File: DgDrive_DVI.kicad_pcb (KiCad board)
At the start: 2 copper layers, 69 x 28 mm, 26 parts, among them J1 Bias-T, J2 DVI-I, J3 Ld+, J4 Ld-, J5 Pz+, J6 Pz-, J7 Piezo_In, K1 G6AU, Q1 MMBT3904, Q2 2N4401

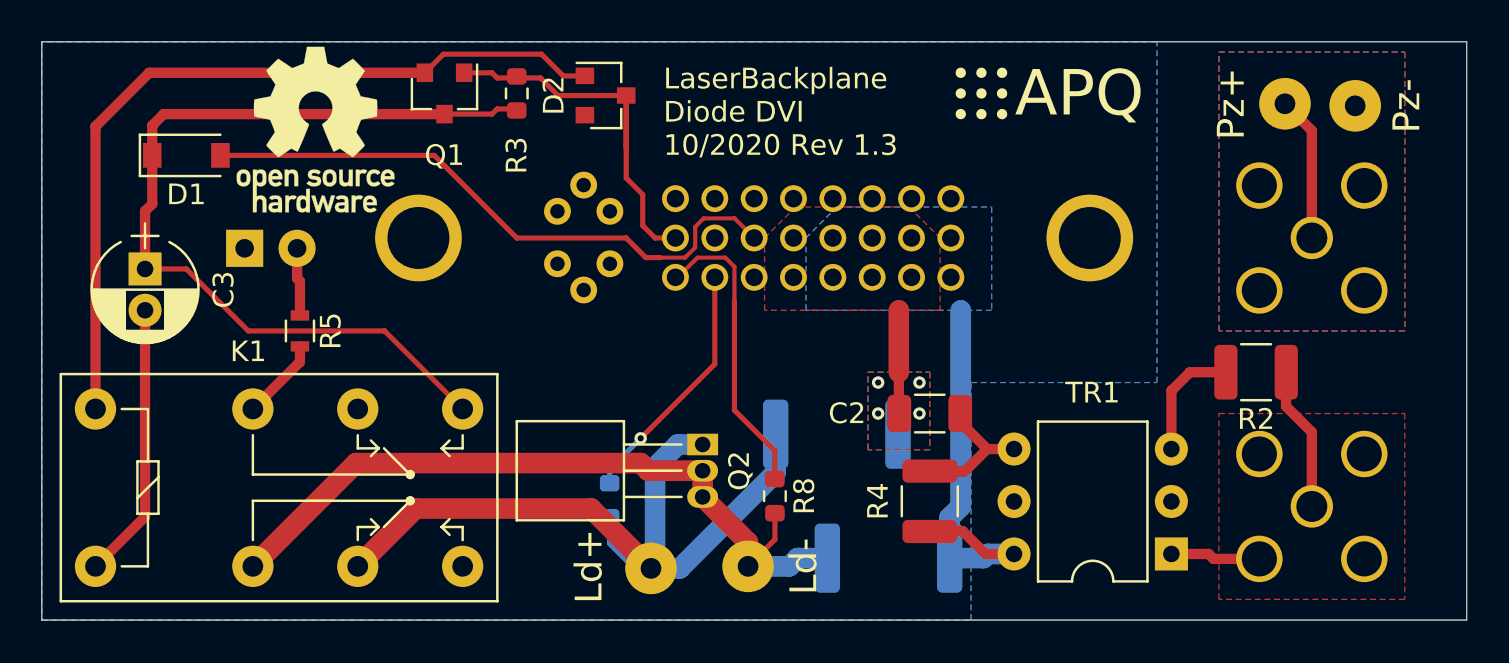
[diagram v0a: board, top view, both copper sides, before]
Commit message: Ld-: SMD Pad for shield
Fix footprints and replace Ld- THT with SMD pad
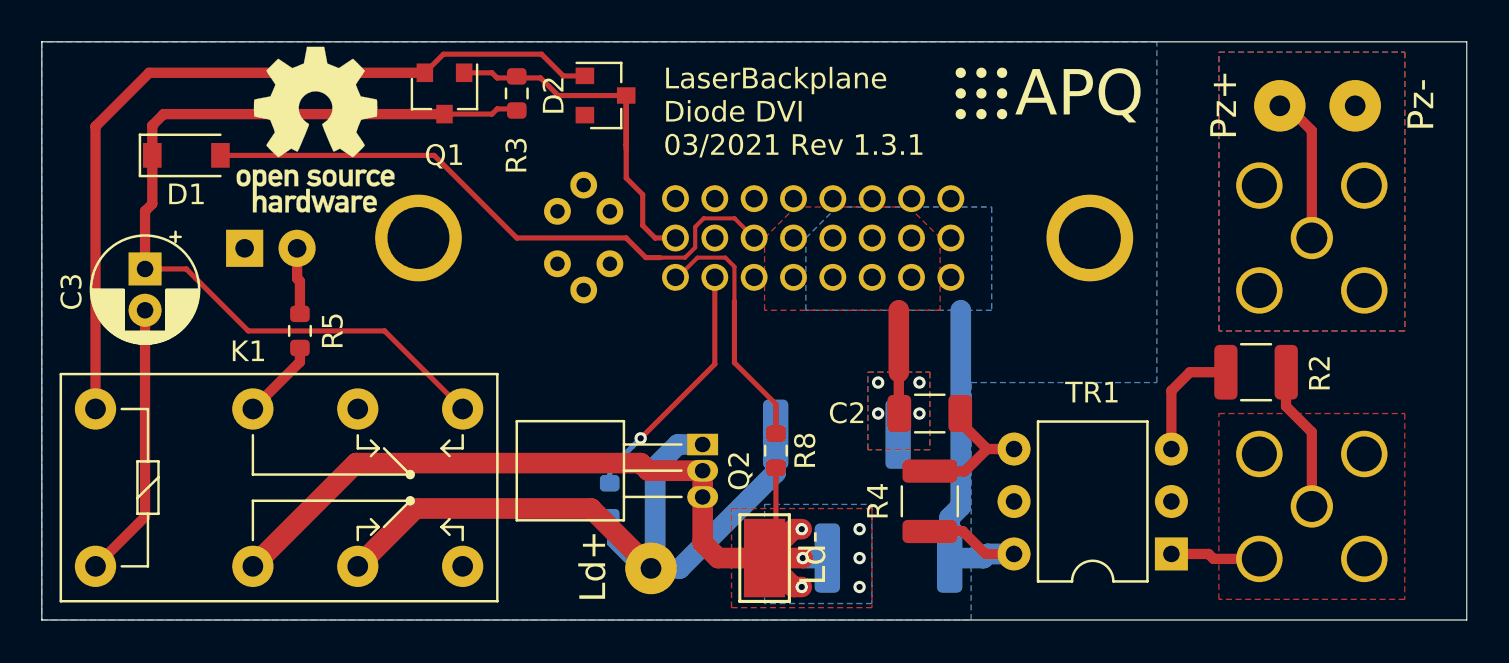
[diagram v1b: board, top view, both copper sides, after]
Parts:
- C3: footprint Capacitors_THT:CP_Radial_D5.0mm_P2.00mm -> Capacitor_THT:CP_Radial_D5.0mm_P2.00mm
- J3, J5, J6: footprint Wire_Pads:SolderWirePad_single_1mmDrill -> Connector_Wire:SolderWirePad_1x01_Drill1mm
- J4: footprint Wire_Pads:SolderWirePad_single_1mmDrill -> TestPoint:TestPoint_Keystone_5019_Minature
- R5: value 2k -> 1k; footprint Resistors_SMD:R_0603 -> Resistor_SMD:R_0603_1608Metric
- moved R8 2.20 mm to (125.5, 109.8)
- moved J4 0.89 mm to (125.0, 115.0), turned to 90 degrees
- moved J5 0.27 mm to (149.9, 93.1)
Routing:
- net LD_short-: track 36.7 -> 45.0 mm, vias 0 -> 6
- net V_diode-: track 14.5 -> 12.4 mm
- added copper zone on B.Cu, net LD_short-
- added copper zone on F.Cu, net LD_short-
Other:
- board text added: "LaserBackplane Diode DVI 03/2021 Rev 1.3.1"
- board text removed: "LaserBackplane Diode DVI 10/2020 Rev 1.3"

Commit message: Add current source
Replace Bias-T with Howland current source. The current source requires additional negative supply (Pin7).

Replace large resistors with inductors+49.9-resistors.
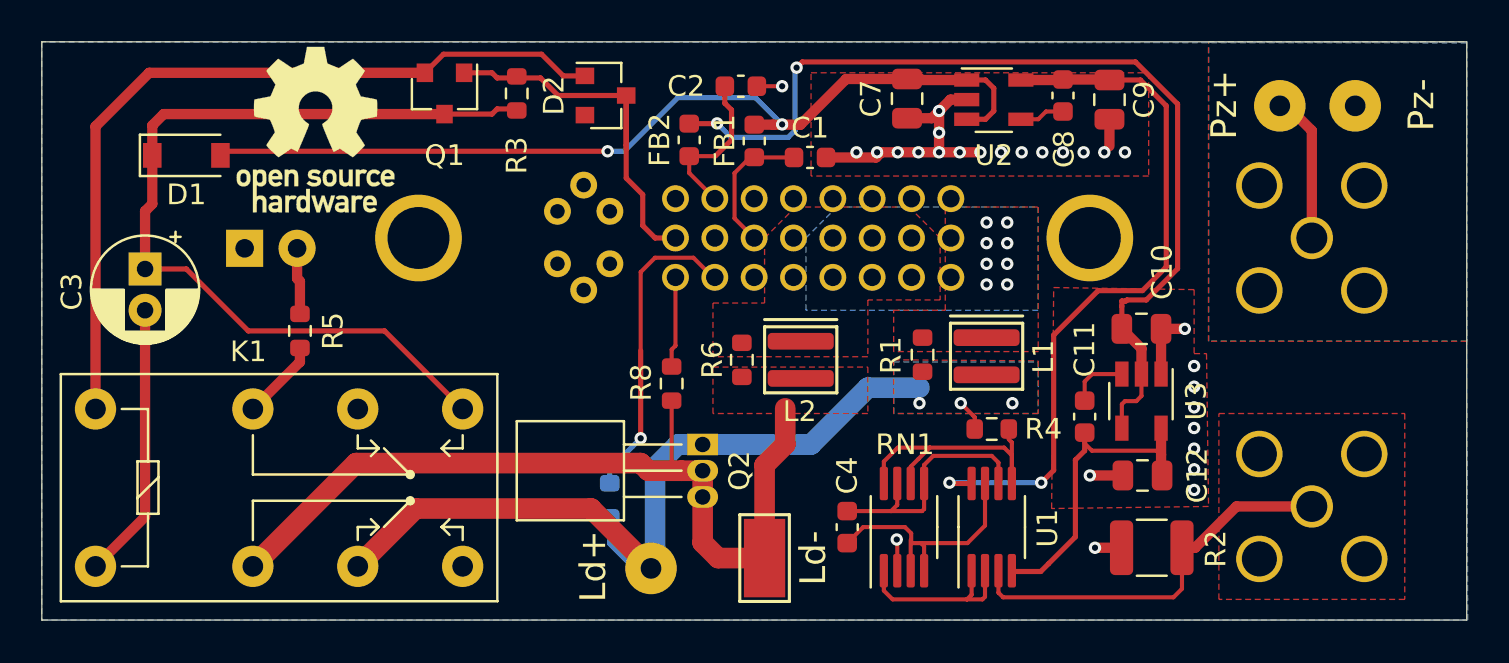
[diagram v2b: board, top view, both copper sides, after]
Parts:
- removed TR1: SWB1010, Package_DIP:DIP-6_W7.62mm
- added C1: 10n, Capacitor_SMD:C_0603_1608Metric, F.Cu at (127.2, 95.6)
- added C10: 4.7u, Capacitor_SMD:C_0805_2012Metric, F.Cu at (143.2, 103.9)
- added C11: 10n, Capacitor_SMD:C_0603_1608Metric, F.Cu at (140.5, 108.2)
- added C12: 4.7u, Capacitor_SMD:C_0805_2012Metric, F.Cu at (143.3, 111.0)
- added C4: 1.5p, Capacitor_SMD:C_0603_1608Metric, F.Cu at (129.0, 113.5)
- added C7: 4.7u, Capacitor_SMD:C_0805_2012Metric, F.Cu at (131.9, 92.8)
- added C8: 10n, Capacitor_SMD:C_0603_1608Metric, F.Cu at (139.4, 92.6)
- added C9: 4.7u, Capacitor_SMD:C_0805_2012Metric, F.Cu at (141.7, 92.8)
- added FB1: BLM18KG102SZ1D, Inductor_SMD:L_0603_1608Metric, F.Cu at (124.5, 94.8)
- added FB2: BLM18KG102SZ1D, Inductor_SMD:L_0603_1608Metric, F.Cu at (121.3, 94.8)
- added L1: 3.3u, custom:Coilcraft_XGL3530, F.Cu at (135.8, 104.3)
- added L2: 3.3u, custom:Coilcraft_XGL3530, F.Cu at (126.8, 104.5)
- added RN1: 10k, custom:MSOP-8_3x3mm_P0.65mm_mod, F.Cu at (131.8, 113.5)
- added U1: ADA4807-2ARM, custom:MSOP-8_3x3mm_P0.65mm_mod, F.Cu at (136.0, 113.5)
- added U2: LT1761-5, Package_TO_SOT_SMD:TSOT-23-5, F.Cu at (136.1, 92.8)
- added U3: LT1964-5, Package_TO_SOT_SMD:TSOT-23-5, F.Cu at (143.2, 107.4)
- C2: value 3.3n (C0G) -> 10n; footprint Capacitor_SMD:C_1206_3216Metric -> Capacitor_SMD:C_0603_1608Metric
- J1: value Bias-T -> Curr. Mod.
- LOGO1: moved to B.Cu
- R1, R6: value 5.6 / 750 mW -> 49.9; footprint Resistor_SMD:R_2512_6332Metric -> Resistor_SMD:R_0603_1608Metric; moved to F.Cu
- R4: value 49.9 -> 10; footprint Resistor_SMD:R_1210_3225Metric -> Resistor_SMD:R_0603_1608Metric
- moved LOGO1 25.5 mm to (144.1, 115.2)
- moved C2 18.3 mm to (123.8, 92.2)
- moved R6 11.9 mm to (123.9, 105.4), turned to 90 degrees
- moved R2 9.89 mm to (143.8, 114.5)
- moved R8 6.01 mm to (120.5, 106.5)
- moved R1 5.66 mm to (132.7, 105.2), turned to 90 degrees
- moved R4 4.61 mm to (136.0, 108.8), turned to 180 degrees
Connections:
- C2 pad 2: Net-(C2-Pad2) -> GND
- D1 pad 2: Relay+ -> +12V
- J1 pad 2: Net-(J1-Pad2) -> GND
- J2 pad 10: Net-(C2-Pad1) -> Net-(J2-Pad10)
- J2 pad 13: Net-(C2-Pad1) -> Net-(J2-Pad10)
- J2 pad 14: Relay+ -> Net-(C1-Pad1)
- J2 pad 7: Net-(J2-Pad7) -> Net-(C2-Pad1)
- J3 pad 1: LD_short+ -> Curr_Mod
- K1 pad 6: LD_short+ -> Curr_Mod
- Q2 pad 1: LD_short+ -> Curr_Mod
- R1 pad 1: LD_short+ -> Curr_Mod
- R1 pad 2: Net-(C2-Pad1) -> Net-(J2-Pad12)
- R2 pad 2: Net-(R2-Pad2) -> GND
- R4 pad 1: Net-(C2-Pad2) -> Net-(R4-Pad1)
- R4 pad 2: Net-(J2-Pad12) -> Curr_Mod
- R6 pad 2: Net-(J2-Pad12) -> Net-(J2-Pad10)
- R7 pad 1: LD_short+ -> Curr_Mod
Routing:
- net -12V: track 0.00 -> 46.6 mm, vias 0 -> 2
- net +12V: track 0.00 -> 44.6 mm, vias 0 -> 2
- net Curr_Mod: track 0.00 -> 41.2 mm, vias 0 -> 3
- net LD_short+: track 37.9 -> 0.00 mm
- net +5V: track 0.00 -> 35.1 mm, vias 0 -> 2
- net Relay+: track 29.7 -> 0.00 mm
- net GND: track 0.00 -> 23.1 mm, vias 0 -> 28
- net Net-(J2-Pad12): track 20.2 -> 0.00 mm, vias 0 -> 8
- net -5V: track 0.00 -> 15.8 mm
- net Net-(R4-Pad1): track 0.00 -> 13.8 mm
- net Net-(C4-Pad1): track 0.00 -> 12.9 mm
- net Net-(J1-Pad1): track 7.02 -> 19.3 mm
- net Net-(C4-Pad2): track 0.00 -> 12.3 mm
- net Net-(RN1-Pad1): track 0.00 -> 8.76 mm
- net V_diode-: track 12.4 -> 4.51 mm
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- added copper zone on B.Cu, net Curr_Mod
- added copper zone on F.Cu, net Curr_Mod
- added copper zone on F.Cu, net GND
- added copper zone on F.Cu, net Net-(J2-Pad10)
- added copper zone on F.Cu, net Net-(J2-Pad12)
- removed copper zone on B.Cu, net LD_short-
- removed copper zone on B.Cu, net Net-(C2-Pad1)
- removed copper zone on F.Cu, net Net-(C2-Pad1)
- removed copper zone on F.Cu, net Net-(J1-Pad2)
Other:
- board text added: "LaserBackplane Diode DVI 03/2021 Rev 1.4"
- board text removed: "Distance of the back side to the case: 0.9 mm"
- board text removed: "LaserBackplane Diode DVI 03/2021 Rev 1.3.1"
- board text removed: "Note: The two big 2512 resistors will be thermally coupled to the case, so they need to be on the back side"

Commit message: Updated Gerber files to 1.4 Added EEPROM
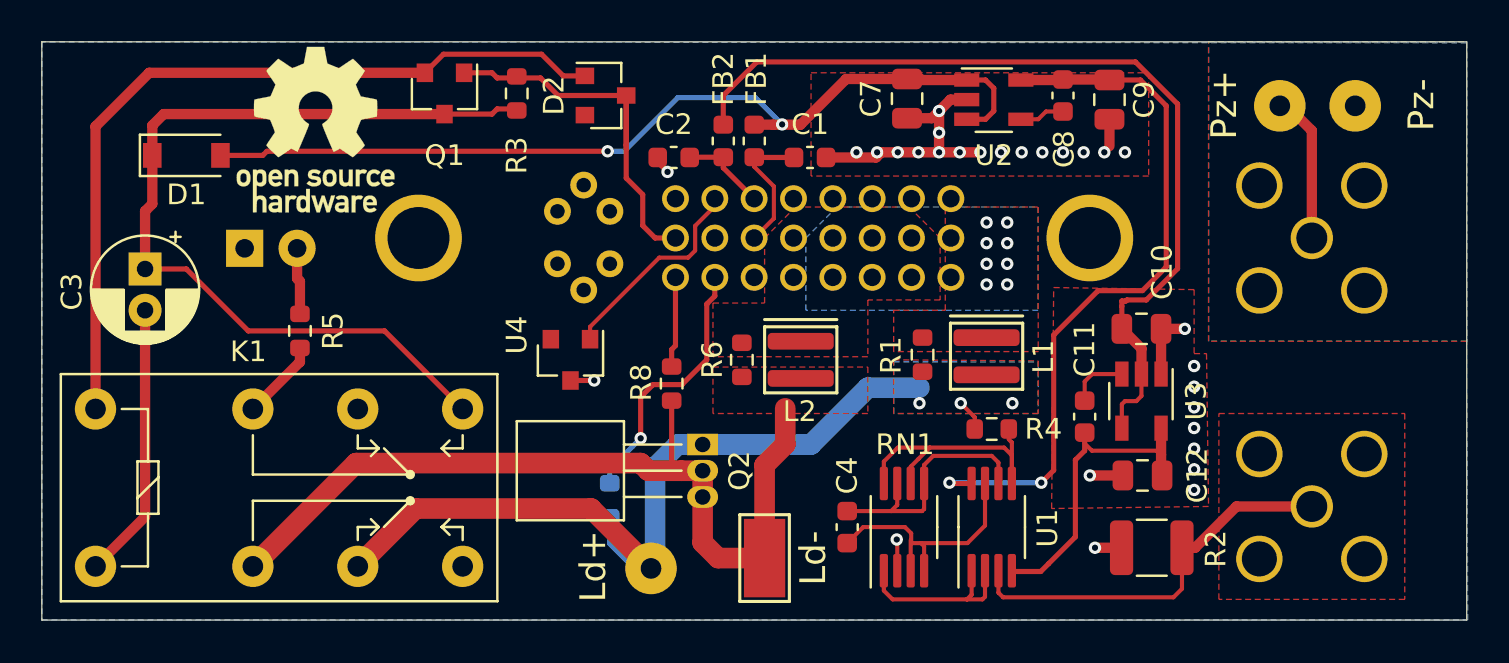
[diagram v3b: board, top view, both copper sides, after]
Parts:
- added U4: AT21CS11-STXXXX-X, Package_TO_SOT_SMD:SOT-23, F.Cu at (115.6, 105.4)
- moved C2 4.74 mm to (120.6, 95.6), turned to 180 degrees
- moved FB2 1.65 mm to (123.0, 94.8)
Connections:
- J2 pad 6: Net-(J2-Pad6) -> Net-(C2-Pad1)
- J2 pad 7: Net-(C2-Pad1) -> Net-(J2-Pad7)
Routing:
- net Net-(J2-Pad7): track 0.00 -> 10.1 mm
- net Net-(C2-Pad1): track 7.68 -> 4.26 mm
- net -12V: track 46.6 -> 43.5 mm, vias 2 -> 0
- net V_diode+: track 15.2 -> 12.9 mm
- net GND: track 23.1 -> 23.9 mm, vias 28 -> 29

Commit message: Fix laser diode polarity
Switch LD-/LD+ pins at the DVI connector
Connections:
- L1 pad 1: Net-(J2-Pad12) -> Net-(J2-Pad10)
- L2 pad 1: Net-(J2-Pad10) -> Net-(J2-Pad12)
- R1 pad 2: Net-(J2-Pad12) -> Net-(J2-Pad10)
- R6 pad 2: Net-(J2-Pad10) -> Net-(J2-Pad12)
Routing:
- net Net-(J2-Pad12): vias 8 -> 0
- net Net-(J2-Pad10): vias 0 -> 8
- added copper zone on B.Cu, net Net-(J2-Pad10)
- removed copper zone on B.Cu, net Net-(J2-Pad12)
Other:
- board text added: "LaserBackplane Diode DVI 07/2021 Rev 1.5"
- board text removed: "LaserBackplane Diode DVI 03/2021 Rev 1.4"

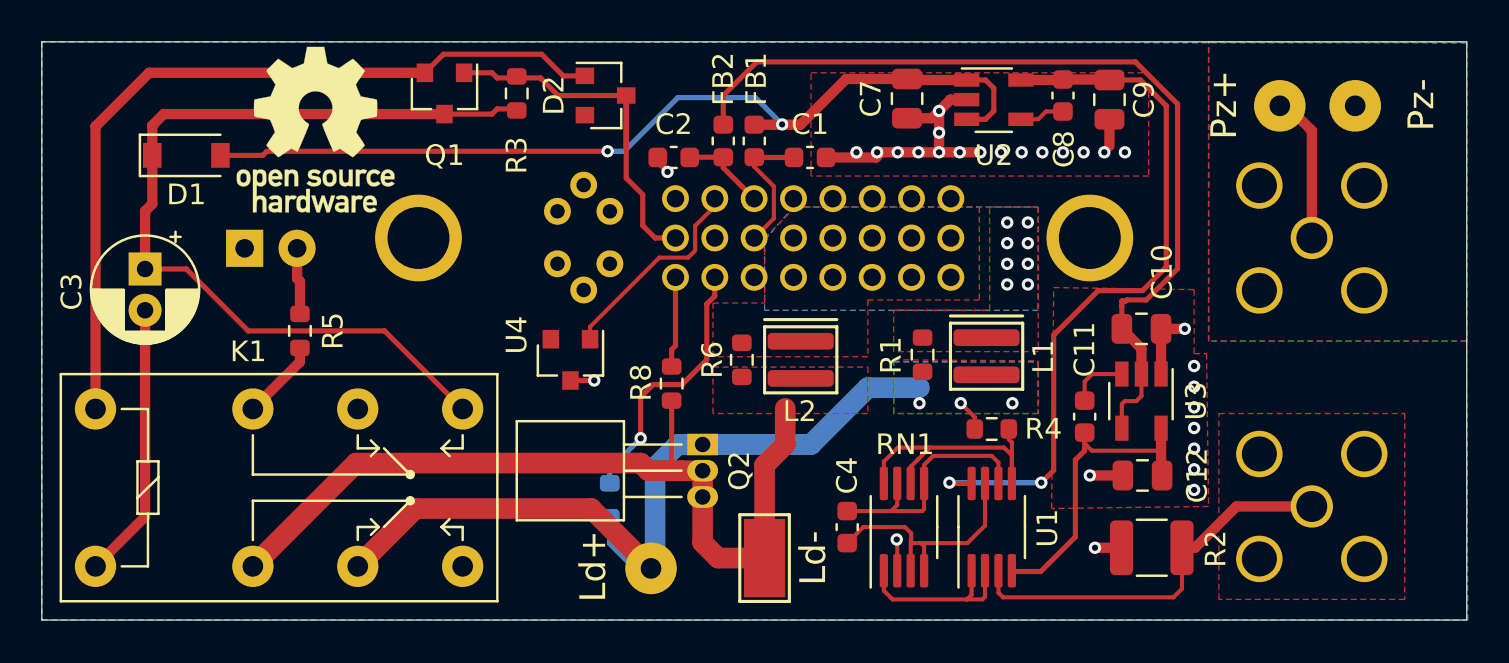
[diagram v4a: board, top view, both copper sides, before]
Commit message: Replace XGL3530 with XGL5050
-Use a larger inductance
-Options for no inductance at LD- and ground referenced design.
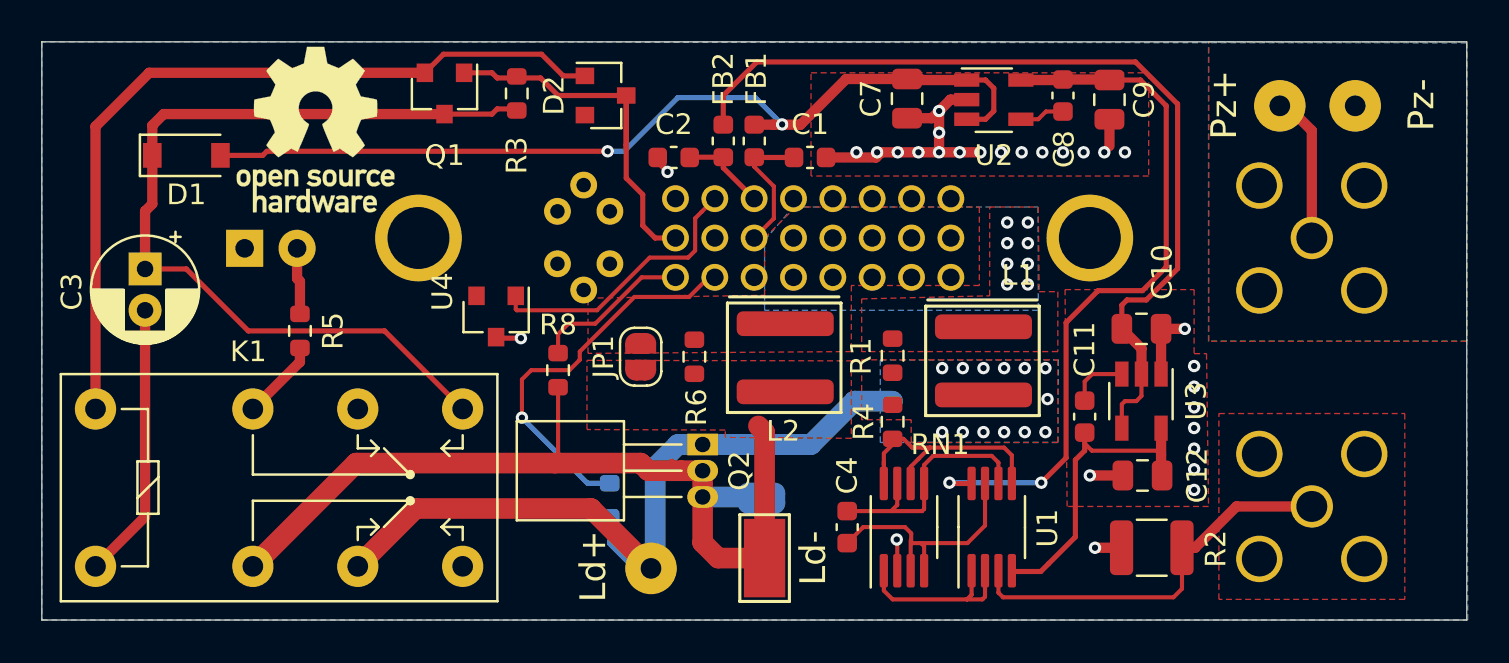
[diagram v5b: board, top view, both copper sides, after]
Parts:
- added JP1: No_L, Jumper:SolderJumper-2_P1.3mm_Open_RoundedPad1.0x1.5mm, F.Cu at (119.0, 105.2)
- added JP2: GND, Jumper:SolderJumper-2_P1.3mm_Open_RoundedPad1.0x1.5mm, B.Cu at (124.8, 112.1)
- L1, L2: value 3.3u -> 33u; footprint custom:Coilcraft_XGL3530 -> custom:Coilcraft_XGL5050
- RN1: value 10k -> 1k
- moved R8 5.54 mm to (115.0, 105.9)
- moved R4 4.81 mm to (131.2, 108.4), turned to 90 degrees
- moved LOGO1 4.45 mm to (144.2, 110.7)
- moved U4 4.17 mm to (112.0, 103.3)
- moved R6 2.30 mm to (121.6, 105.2)
- moved R1 1.45 mm to (131.2, 105.2)
- moved L2 1.13 mm to (126.0, 103.7)
- moved L1 0.55 mm to (135.6, 103.8)
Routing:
- net V_diode+: track 12.9 -> 19.3 mm
- net V_diode-: track 4.40 -> 8.01 mm
- net Net-(J2-Pad7): track 10.1 -> 13.5 mm
- net Curr_Mod: track 41.2 -> 38.1 mm, vias 3 -> 13
- net LD_short-: track 44.7 -> 46.9 mm
- net Net-(R4-Pad1): track 13.8 -> 12.0 mm

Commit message: Remove L2
Remove inductance and bypass resistor at Ld-.
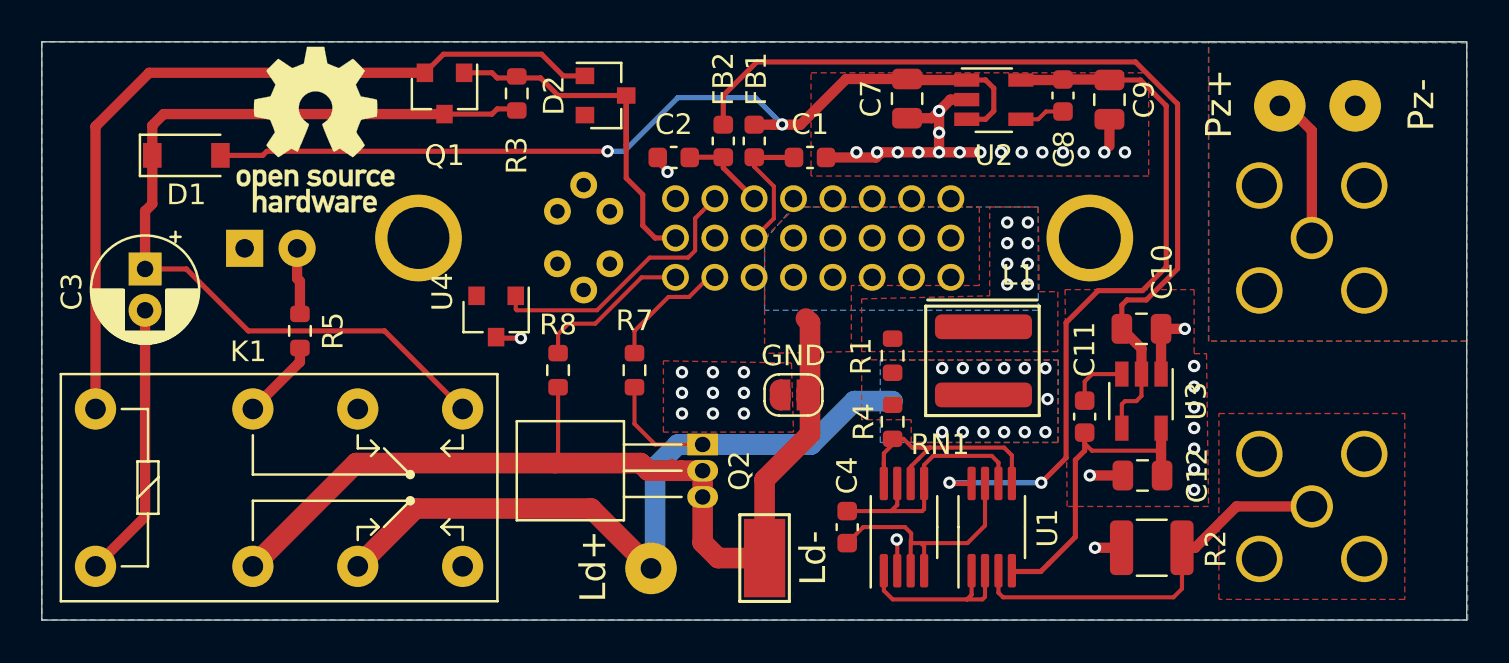
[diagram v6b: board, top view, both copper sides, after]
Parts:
- removed JP1: No_L, Jumper:SolderJumper-2_P1.3mm_Open_RoundedPad1.0x1.5mm
- removed L2: 33u, custom:Coilcraft_XGL5050
- removed R6: 49.9, Resistor_SMD:R_0603_1608Metric
- JP2, R7: moved to F.Cu
- moved R7 6.41 mm to (118.7, 105.9)
- moved JP2 5.23 mm to (126.4, 107.1), turned to 180 degrees
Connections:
- J2 pad 12: Net-(J2-Pad12) -> LD_short-
- J2 pad 9: Net-(J2-Pad12) -> LD_short-
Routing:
- net V_diode+: track 19.3 -> 6.15 mm, vias 1 -> 0
- net LD_short-: track 46.9 -> 50.8 mm
- net Curr_Mod: track 38.1 -> 40.7 mm
- net GND: vias 29 -> 38
- removed copper zone on F.Cu, net Net-(J2-Pad12)
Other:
- board text added: "LaserBackplane Diode DVI 10/2021 Rev 1.6"
- board text removed: "LaserBackplane Diode DVI 07/2021 Rev 1.5"
